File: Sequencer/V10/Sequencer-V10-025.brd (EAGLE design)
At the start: 100 x 48 mm, 42 parts, among them IC2 LD117ADT50TR, IC6 LM1117MPX-ADJ, Q1 IRF530, X1 MARTIN8X2-1751303, X2 MARTIN3X2-1751303175L303-3, X3 MARTIN8X2-1751303, X4 1751264, X5 MARTIN3X2-1751303175L303-3

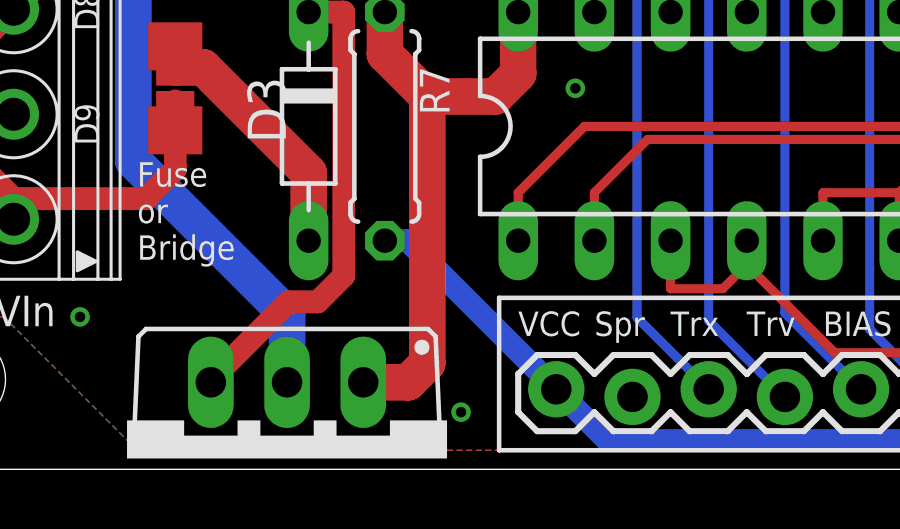
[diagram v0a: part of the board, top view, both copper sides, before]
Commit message: Fix MOSFET to UREG
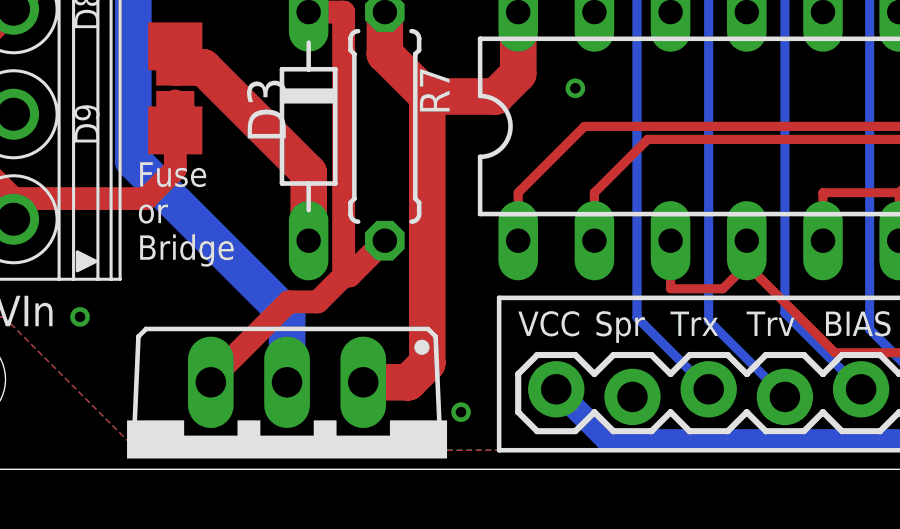
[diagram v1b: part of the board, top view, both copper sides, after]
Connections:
- net UREG: now also R7.2
- net VCC: no longer R7.2
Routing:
- net VCC: track 192.5 -> 184.7 mm
- net UREG: track 115.4 -> 117.3 mm
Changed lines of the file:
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@@
 <wire x1="15.266" y1="25.711" x2="15.235" y2="25.68" width="0.762" layer="1"/>
 <wire x1="41.91" y1="15.24" x2="41.91" y2="17.0689" width="0.762" layer="1"/>
+<contactref element="R7" pad="2"/>
+<wire x1="17.145" y1="7.62" x2="15.9715" y2="6.4465" width="0.762" layer="1"/>
+<wire x1="15.9715" y1="6.4465" x2="15.7735" y2="6.4465" width="0.762" layer="1"/>
 </signal>
 <signal name="VCC" class="1">
@@
 <wire x1="69.95" y1="35.915" x2="73.125" y2="32.74" width="0.762" layer="16"/>
 <wire x1="73.125" y1="32.74" x2="73.125" y2="30.675" width="0.762" layer="16"/>
-<contactref element="R7" pad="2"/>
-<wire x1="22.86" y1="2.667" x2="17.907" y2="7.62" width="0.762" layer="16"/>
-<wire x1="17.907" y1="7.62" x2="17.145" y2="7.62" width="0.762" layer="16"/>
 </signal>
 <signal name="A4" class="2">
